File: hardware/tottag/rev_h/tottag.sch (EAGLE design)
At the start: 199 parts, among them J1 USB4110-GF-A, J2 DM3AT-SF-PEJM5, J3 TC2030-JLINK-NL-2SIDE, J4 TC2030-JLINK-NL-2SIDE, J5 MOLEX-PICO-SPOX-3SIDE, Q1 CSD75207W15, Q2 CSD75207W15, T1 HHM1595A1, U1 DW1000, U10 STM32F091CC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

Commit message: rev_h: split SPI buses; replace coil
Pin updates from SPI reconfiguration:

    SPI0 (Accelerometer)
        SCLK: P0.17
        MISO: P0.15
        MOSI: P0.13
        (INT, CS pins unchanged)
    SPI2 (RTC, SD Card)
        SCLK: P0.06
        MOSI: P0.07
        MISO: P0.05
        (CS, detect, etc pins unchanged)
    BATIN moved to P0.04 (to simplify routing)

---

Coil replaced with new part; slightly wider holes, adjusted fill to fit

(was meant to be its own commit; oh well)
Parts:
- L4: value WR222230-26M8-G -> WURTH_COIL_760308103204; device ac:WR222230-26M8-G -> ac:WURTH_COIL_760308103204
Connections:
- removed net NRF_MISO: J2.DATA0/MISO, R32.1, U11.SDO, U3.MISO/SA0, U7.P0.15
- removed net NRF_MOSI: J2.CMD/MOSI, R30.1, U11.SDI, U3.MOSI/SDA, U7.P0.13
- removed net NRF_SCK: J2.CLK, U11.SCL, U3.SCL/SPC, U7.P0.17
- new net NRF_SPI0_MISO: U3.MISO/SA0, U7.P0.15
- new net NRF_SPI0_MOSI: U3.MOSI/SDA, U7.P0.13
- new net NRF_SPI0_SCLK: U3.SCL/SPC, U7.P0.17
- new net NRF_SPI2_MISO: J2.DATA0/MISO, R32.1, U11.SDO, U7.P0.05/AIN3
- new net NRF_SPI2_MOSI: J2.CMD/MOSI, R30.1, U11.SDI, U7.P0.07
- new net NRF_SPI2_SCLK: J2.CLK, U11.SCL, U7.P0.06
- net BATIN: now also U7.P0.04/AIN2; no longer U7.P0.30*/AIN6
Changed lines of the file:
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@@
 <attribute name="MPN" value="GRM1555C1H471JA01J"/>
 </part>
-<part name="L4" library="ac" library_urn="urn:adsk.eagle:library:20878999" deviceset="WR222230-26M8-G" device="" package3d_urn="urn:adsk.eagle:package:20906931/3"/>
+<part name="L4" library="ac" library_urn="urn:adsk.eagle:library:20878999" deviceset="WURTH_COIL_760308103204" device="" package3d_urn="urn:adsk.eagle:package:26902695/1"/>
 <part name="R18" library="passives" library_urn="urn:adsk.eagle:library:20904581" deviceset="RESISTOR" device="0402_RES" package3d_urn="urn:adsk.eagle:package:20904668/2" value="5.1k">
 <attribute name="DIGIKEY" value="RMCF0402FT5K10CT-ND"/>
@@
 </segment>
 </net>
-<net name="NRF_MISO" class="0">
-<segment>
-<pinref part="U7" gate="G$1" pin="P0.15"/>
-<wire x1="60.96" y1="68.58" x2="55.88" y2="68.58" width="0.1524" layer="91"/>
-<label x="55.88" y="68.58" size="1.27" layer="95" rot="R180" xref="yes"/>
-</segment>
+<net name="NRF_SPI2_MISO" class="0">
 <segment>
 <pinref part="U11" gate="G$1" pin="SDO"/>
@@
 <label x="182.88" y="93.98" size="1.27" layer="95" rot="R180" xref="yes"/>
 </segment>
-</net>
-<net name="NRF_MOSI" class="0">
-<segment>
-<label x="55.88" y="73.66" size="1.27" layer="95" rot="R180" xref="yes"/>
-<pinref part="U7" gate="G$1" pin="P0.13"/>
-<wire x1="60.96" y1="73.66" x2="55.88" y2="73.66" width="0.1524" layer="91"/>
-</segment>
+<segment>
+<label x="111.76" y="124.46" size="1.27" layer="95" xref="yes"/>
+<wire x1="111.76" y1="124.46" x2="106.68" y2="124.46" width="0.1524" layer="91"/>
+<pinref part="U7" gate="G$1" pin="P0.05/AIN3"/>
+</segment>
+</net>
+<net name="NRF_SPI2_MOSI" class="0">
 <segment>
 <pinref part="U11" gate="G$1" pin="SDI"/>
@@
 <label x="182.88" y="91.44" size="1.27" layer="95" rot="R180" xref="yes"/>
 </segment>
-</net>
-<net name="NRF_SCK" class="0">
-<segment>
-<pinref part="U7" gate="G$1" pin="P0.17"/>
-<wire x1="60.96" y1="63.5" x2="55.88" y2="63.5" width="0.1524" layer="91"/>
-<label x="55.88" y="63.5" size="1.27" layer="95" rot="R180" xref="yes"/>
-</segment>
+<segment>
+<pinref part="U7" gate="G$1" pin="P0.07"/>
+<wire x1="55.88" y1="83.82" x2="60.96" y2="83.82" width="0.1524" layer="91"/>
+<label x="55.88" y="83.82" size="1.27" layer="95" rot="R180" xref="yes"/>
+</segment>
+</net>
+<net name="NRF_SPI2_SCLK" class="0">
 <segment>
 <pinref part="U11" gate="G$1" pin="SCL"/>
 <wire x1="187.96" y1="96.52" x2="182.88" y2="96.52" width="0.1524" layer="91"/>
 <label x="182.88" y="96.52" size="1.27" layer="95" rot="R180" xref="yes"/>
+</segment>
+<segment>
+<pinref part="U7" gate="G$1" pin="P0.06"/>
+<wire x1="55.88" y1="86.36" x2="60.96" y2="86.36" width="0.1524" layer="91"/>
+<label x="55.88" y="86.36" size="1.27" layer="95" rot="R180" xref="yes"/>
 </segment>
 </net>
@@
 <net name="BATIN" class="0">
 <segment>
-<pinref part="U7" gate="G$1" pin="P0.30*/AIN6"/>
-<wire x1="106.68" y1="116.84" x2="111.76" y2="116.84" width="0.1524" layer="91"/>
-<label x="111.76" y="116.84" size="1.27" layer="95" xref="yes"/>
+<label x="111.76" y="127" size="1.27" layer="95" xref="yes"/>
+<pinref part="U7" gate="G$1" pin="P0.04/AIN2"/>
+<wire x1="106.68" y1="127" x2="111.76" y2="127" width="0.1524" layer="91"/>
 </segment>
 </net>
@@
 <label x="55.88" y="78.74" size="1.27" layer="95" rot="R180" xref="yes"/>
 <pinref part="U7" gate="G$1" pin="P0.11"/>
+</segment>
+</net>
+<net name="NRF_SPI0_SCLK" class="0">
+<segment>
+<pinref part="U7" gate="G$1" pin="P0.17"/>
+<wire x1="55.88" y1="63.5" x2="60.96" y2="63.5" width="0.1524" layer="91"/>
+<label x="55.88" y="63.5" size="1.27" layer="95" rot="R180" xref="yes"/>
+</segment>
+</net>
+<net name="NRF_SPI0_MOSI" class="0">
+<segment>
+<pinref part="U7" gate="G$1" pin="P0.13"/>
+<wire x1="55.88" y1="73.66" x2="60.96" y2="73.66" width="0.1524" layer="91"/>
+<label x="55.88" y="73.66" size="1.27" layer="95" rot="R180" xref="yes"/>
+</segment>
+</net>
+<net name="NRF_SPI0_MISO" class="0">
+<segment>
+<pinref part="U7" gate="G$1" pin="P0.15"/>
+<wire x1="55.88" y1="68.58" x2="60.96" y2="68.58" width="0.1524" layer="91"/>
+<label x="55.88" y="68.58" size="1.27" layer="95" rot="R180" xref="yes"/>
 </segment>
 </net>
@@
 </segment>
 </net>
-<net name="NRF_MOSI" class="0">
-<segment>
-<pinref part="U3" gate="G$1" pin="MOSI/SDA"/>
-<wire x1="195.58" y1="35.56" x2="193.04" y2="35.56" width="0.1524" layer="91"/>
-<label x="193.04" y="35.56" size="1.27" layer="95" rot="R180" xref="yes"/>
-</segment>
+<net name="NRF_SPI2_MOSI" class="0">
 <segment>
 <pinref part="J2" gate="G$1" pin="CMD/MOSI"/>
@@
 </segment>
 </net>
-<net name="NRF_MISO" class="0">
-<segment>
-<pinref part="U3" gate="G$1" pin="MISO/SA0"/>
-<wire x1="195.58" y1="38.1" x2="193.04" y2="38.1" width="0.1524" layer="91"/>
-<label x="193.04" y="38.1" size="1.27" layer="95" rot="R180" xref="yes"/>
-</segment>
+<net name="NRF_SPI2_MISO" class="0">
 <segment>
 <pinref part="J2" gate="G$1" pin="DATA0/MISO"/>
@@
 </segment>
 </net>
-<net name="NRF_SCK" class="0">
-<segment>
-<pinref part="U3" gate="G$1" pin="SCL/SPC"/>
-<wire x1="195.58" y1="43.18" x2="193.04" y2="43.18" width="0.1524" layer="91"/>
-<label x="193.04" y="43.18" size="1.27" layer="95" rot="R180" xref="yes"/>
-</segment>
+<net name="NRF_SPI2_SCLK" class="0">
 <segment>
 <pinref part="J2" gate="G$1" pin="CLK"/>
@@
 </segment>
 </net>
+<net name="NRF_SPI0_SCLK" class="0">
+<segment>
+<pinref part="U3" gate="G$1" pin="SCL/SPC"/>
+<wire x1="193.04" y1="43.18" x2="195.58" y2="43.18" width="0.1524" layer="91"/>
+<label x="193.04" y="43.18" size="1.27" layer="95" rot="R180" xref="yes"/>
+</segment>
+</net>
+<net name="NRF_SPI0_MISO" class="0">
+<segment>
+<pinref part="U3" gate="G$1" pin="MISO/SA0"/>
+<wire x1="193.04" y1="38.1" x2="195.58" y2="38.1" width="0.1524" layer="91"/>
+<label x="193.04" y="38.1" size="1.27" layer="95" rot="R180" xref="yes"/>
+</segment>
+</net>
+<net name="NRF_SPI0_MOSI" class="0">
+<segment>
+<pinref part="U3" gate="G$1" pin="MOSI/SDA"/>
+<wire x1="193.04" y1="35.56" x2="195.58" y2="35.56" width="0.1524" layer="91"/>
+<label x="193.04" y="35.56" size="1.27" layer="95" rot="R180" xref="yes"/>
+</segment>
+</net>

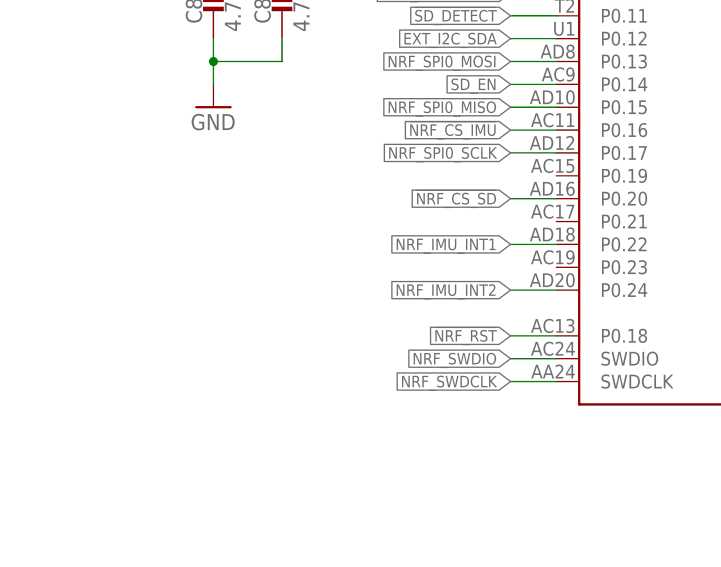
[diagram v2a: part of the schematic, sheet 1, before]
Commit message: rev_h: add board ID pins
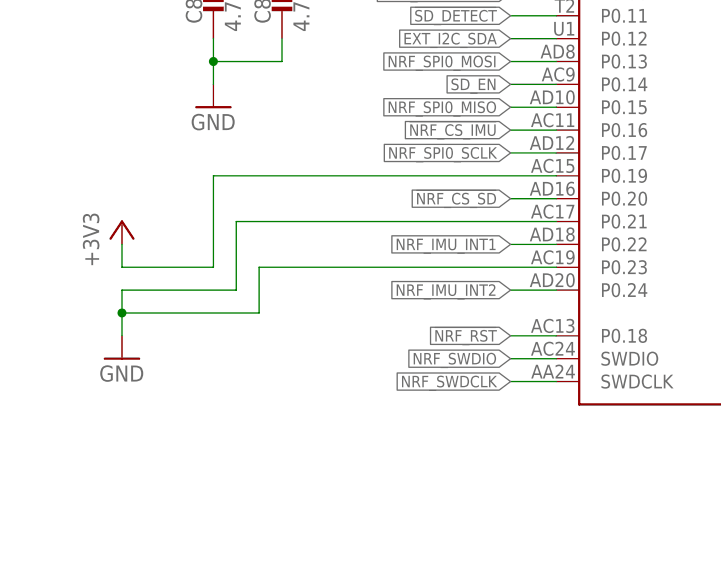
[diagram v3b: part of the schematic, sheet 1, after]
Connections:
- net +3V3: now also U7.P0.19
- net GND: now also U7.P0.21, U7.P0.23
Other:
- note added: "Board Revision ID Pins Rev H = 001"
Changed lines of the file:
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@@
 <part name="TP17" library="headers" deviceset="TEST-POINT" device=""/>
 <part name="TP18" library="headers" deviceset="TEST-POINT" device=""/>
+<part name="P+6" library="regulators" deviceset="+3V3" device=""/>
+<part name="GND9" library="supply1" library_urn="urn:adsk.eagle:library:371" deviceset="GND" device=""/>
 </parts>
 <sheets>
@@
 <text x="143.256" y="27.178" size="1.016" layer="98" align="top-left">Matching network from datasheet.
 Note v1.1 datasheet updated values.</text>
+<text x="11.176" y="34.798" size="1.016" layer="98" align="top-center">Board Revision ID Pins
+Rev H = 001
+</text>
+<wire x1="2.54" y1="30.48" x2="2.54" y2="58.42" width="0.1524" layer="98" style="longdash"/>
+<wire x1="19.304" y1="30.48" x2="19.304" y2="58.42" width="0.1524" layer="98" style="longdash"/>
+<wire x1="19.304" y1="30.48" x2="2.54" y2="30.48" width="0.1524" layer="98" style="longdash"/>
+<wire x1="19.304" y1="58.42" x2="2.54" y2="58.42" width="0.1524" layer="98" style="longdash"/>
 </plain>
 <instances>
@@
 <instance part="TP18" gate="G$1" x="213.36" y="170.18" smashed="yes" rot="R90">
 <attribute name="NAME" x="213.36" y="169.545" size="1.016" layer="95" ratio="12" rot="R90" align="center-right"/>
+</instance>
+<instance part="P+6" gate="P1" x="12.7" y="55.88" smashed="yes">
+<attribute name="VALUE" x="10.16" y="50.8" size="1.778" layer="96" rot="R90"/>
+</instance>
+<instance part="GND9" gate="1" x="12.7" y="40.64" smashed="yes">
+<attribute name="VALUE" x="10.16" y="38.1" size="1.778" layer="96"/>
 </instance>
 </instances>
@@
 <wire x1="30.48" y1="73.66" x2="22.86" y2="73.66" width="0.1524" layer="91"/>
 <junction x="22.86" y="73.66"/>
+</segment>
+<segment>
+<pinref part="U7" gate="G$1" pin="P0.23"/>
+<wire x1="60.96" y1="50.8" x2="27.94" y2="50.8" width="0.1524" layer="91"/>
+<wire x1="27.94" y1="50.8" x2="27.94" y2="45.72" width="0.1524" layer="91"/>
+<wire x1="27.94" y1="45.72" x2="12.7" y2="45.72" width="0.1524" layer="91"/>
+<pinref part="GND9" gate="1" pin="GND"/>
+<wire x1="12.7" y1="45.72" x2="12.7" y2="43.18" width="0.1524" layer="91"/>
+<pinref part="U7" gate="G$1" pin="P0.21"/>
+<wire x1="60.96" y1="55.88" x2="25.4" y2="55.88" width="0.1524" layer="91"/>
+<wire x1="25.4" y1="55.88" x2="25.4" y2="48.26" width="0.1524" layer="91"/>
+<wire x1="25.4" y1="48.26" x2="12.7" y2="48.26" width="0.1524" layer="91"/>
+<wire x1="12.7" y1="48.26" x2="12.7" y2="45.72" width="0.1524" layer="91"/>
+<junction x="12.7" y="45.72"/>
 </segment>
 </net>
@@
 <junction x="236.22" y="66.04"/>
 </segment>
+<segment>
+<pinref part="U7" gate="G$1" pin="P0.19"/>
+<wire x1="60.96" y1="60.96" x2="22.86" y2="60.96" width="0.1524" layer="91"/>
+<wire x1="22.86" y1="60.96" x2="22.86" y2="50.8" width="0.1524" layer="91"/>
+<wire x1="22.86" y1="50.8" x2="12.7" y2="50.8" width="0.1524" layer="91"/>
+<pinref part="P+6" gate="P1" pin="+3V3"/>
+<wire x1="12.7" y1="50.8" x2="12.7" y2="53.34" width="0.1524" layer="91"/>
+</segment>
 </net>

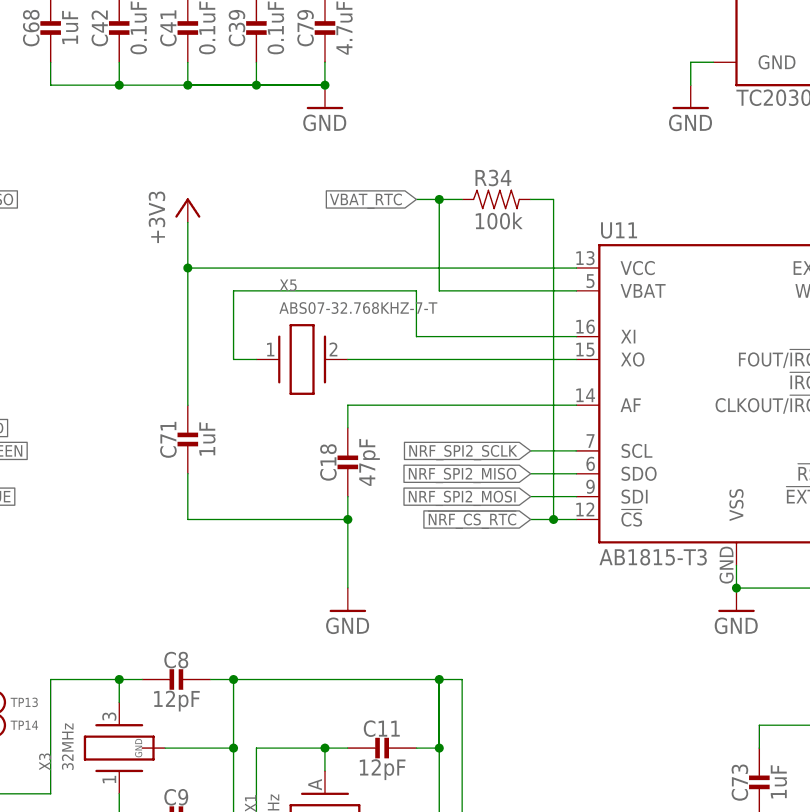
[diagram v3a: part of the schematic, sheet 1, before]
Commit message: rev_h: RTC CS pull-up to +3v3
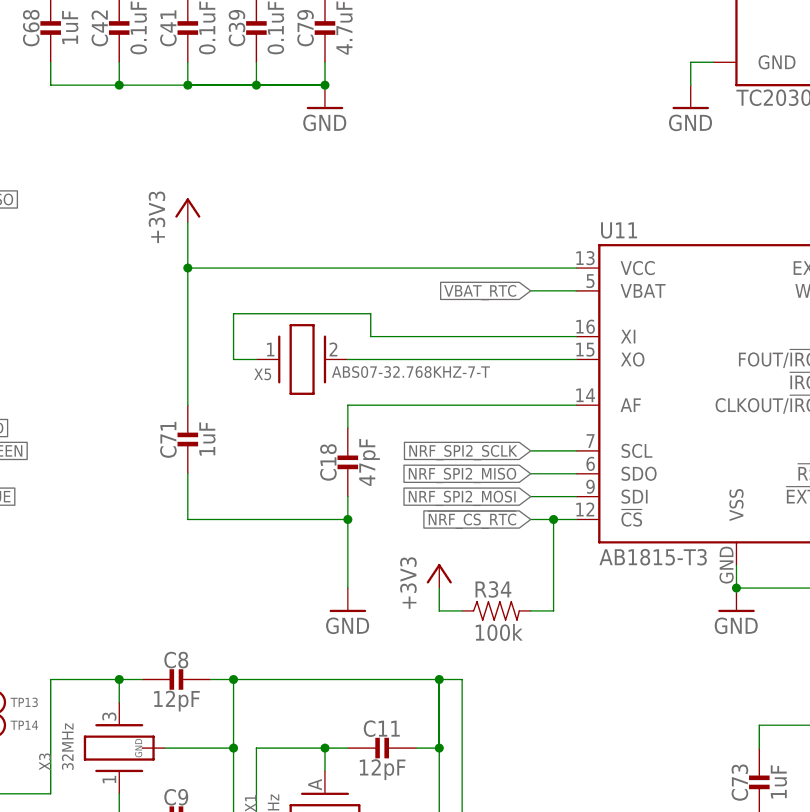
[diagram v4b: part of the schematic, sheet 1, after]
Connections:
- net +3V3: now also R34.1
- net VBAT_RTC: no longer R34.1
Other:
- moved on the sheet: R34
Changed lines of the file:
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@@
 <part name="P+6" library="regulators" deviceset="+3V3" device=""/>
 <part name="GND9" library="supply1" library_urn="urn:adsk.eagle:library:371" deviceset="GND" device=""/>
+<part name="P+7" library="regulators" deviceset="+3V3" device=""/>
 </parts>
 <sheets>
@@
 <wire x1="177.8" y1="165.1" x2="177.8" y2="129.54" width="0.1524" layer="98" style="longdash"/>
 <wire x1="177.8" y1="129.54" x2="254" y2="129.54" width="0.1524" layer="98" style="longdash"/>
-<text x="142.24" y="78.74" size="3.81" layer="98">RTC</text>
-<wire x1="177.8" y1="129.54" x2="134.62" y2="129.54" width="0.1524" layer="98" style="longdash"/>
-<wire x1="134.62" y1="129.54" x2="134.62" y2="74.93" width="0.1524" layer="98" style="longdash"/>
-<wire x1="134.62" y1="74.93" x2="254" y2="74.93" width="0.1524" layer="98" style="longdash"/>
+<text x="149.86" y="121.92" size="3.81" layer="98">RTC</text>
+<wire x1="177.8" y1="129.54" x2="137.16" y2="129.54" width="0.1524" layer="98" style="longdash"/>
+<wire x1="137.16" y1="129.54" x2="137.16" y2="74.93" width="0.1524" layer="98" style="longdash"/>
+<wire x1="137.16" y1="74.93" x2="254" y2="74.93" width="0.1524" layer="98" style="longdash"/>
 <text x="180.34" y="160.02" size="3.81" layer="98">J-LINK</text>
 <text x="178.816" y="166.37" size="3.81" layer="98">LED</text>
-<text x="190.5" y="124.968" size="1.778" layer="98">Pull-up nCS to prevent float</text>
+<text x="169.926" y="86.106" size="0.8128" layer="98">Pull-up nCS to prevent float</text>
 <text x="198.12" y="160.02" size="1.778" layer="98">x2 (top/bottom)</text>
 <text x="205.74" y="68.58" size="3.81" layer="98">Buzzer</text>
@@
 </instance>
 <instance part="X5" gate="G$1" x="157.48" y="106.68" smashed="yes">
-<attribute name="NAME" x="154.94" y="114.3" size="1.27" layer="95"/>
-<attribute name="VALUE" x="154.94" y="111.76" size="1.27" layer="96"/>
+<attribute name="NAME" x="154.178" y="105.664" size="1.27" layer="95" rot="R180"/>
+<attribute name="VALUE" x="160.782" y="104.648" size="1.27" layer="96"/>
 </instance>
 <instance part="C71" gate="G$1" x="144.78" y="99.06" smashed="yes">
@@
 <attribute name="MPN" x="238.76" y="58.42" size="1.27" layer="96" rot="R90" display="off"/>
 </instance>
-<instance part="R34" gate="G$1" x="180.34" y="124.46" smashed="yes">
-<attribute name="NAME" x="176.53" y="125.9586" size="1.778" layer="95"/>
-<attribute name="VALUE" x="176.53" y="121.158" size="1.778" layer="96"/>
+<instance part="R34" gate="G$1" x="180.34" y="78.74" smashed="yes">
+<attribute name="NAME" x="176.53" y="80.2386" size="1.778" layer="95"/>
+<attribute name="VALUE" x="176.53" y="75.438" size="1.778" layer="96"/>
 </instance>
 <instance part="A4" gate="G$1" x="185.42" y="48.26" smashed="yes">
@@
 <instance part="GND9" gate="1" x="12.7" y="40.64" smashed="yes">
 <attribute name="VALUE" x="10.16" y="38.1" size="1.778" layer="96"/>
+</instance>
+<instance part="P+7" gate="P1" x="172.72" y="83.82" smashed="yes">
+<attribute name="VALUE" x="170.18" y="78.74" size="1.778" layer="96" rot="R90"/>
 </instance>
 </instances>
@@
 <wire x1="12.7" y1="50.8" x2="12.7" y2="53.34" width="0.1524" layer="91"/>
 </segment>
+<segment>
+<pinref part="R34" gate="G$1" pin="1"/>
+<pinref part="P+7" gate="P1" pin="+3V3"/>
+<wire x1="175.26" y1="78.74" x2="172.72" y2="78.74" width="0.1524" layer="91"/>
+<wire x1="172.72" y1="78.74" x2="172.72" y2="81.28" width="0.1524" layer="91"/>
+</segment>
 </net>
 <net name="EXT_I2C_SDA" class="0">
@@
 <net name="N$41" class="0">
 <segment>
-<wire x1="149.86" y1="114.3" x2="170.18" y2="114.3" width="0.1524" layer="91"/>
-<wire x1="170.18" y1="114.3" x2="170.18" y2="109.22" width="0.1524" layer="91"/>
+<wire x1="149.86" y1="111.76" x2="165.1" y2="111.76" width="0.1524" layer="91"/>
+<wire x1="165.1" y1="111.76" x2="165.1" y2="109.22" width="0.1524" layer="91"/>
 <pinref part="U11" gate="G$1" pin="XI"/>
-<wire x1="170.18" y1="109.22" x2="187.96" y2="109.22" width="0.1524" layer="91"/>
+<wire x1="165.1" y1="109.22" x2="187.96" y2="109.22" width="0.1524" layer="91"/>
 <pinref part="X5" gate="G$1" pin="1"/>
-<wire x1="149.86" y1="114.3" x2="149.86" y2="106.68" width="0.1524" layer="91"/>
+<wire x1="149.86" y1="111.76" x2="149.86" y2="106.68" width="0.1524" layer="91"/>
 <wire x1="149.86" y1="106.68" x2="152.4" y2="106.68" width="0.1524" layer="91"/>
 </segment>
@@
 <label x="182.88" y="88.9" size="1.27" layer="95" rot="R180" xref="yes"/>
 <wire x1="185.42" y1="88.9" x2="182.88" y2="88.9" width="0.1524" layer="91"/>
-<wire x1="182.88" y1="124.46" x2="185.42" y2="124.46" width="0.1524" layer="91"/>
-<wire x1="185.42" y1="124.46" x2="185.42" y2="88.9" width="0.1524" layer="91"/>
+<wire x1="182.88" y1="78.74" x2="185.42" y2="78.74" width="0.1524" layer="91"/>
+<wire x1="185.42" y1="78.74" x2="185.42" y2="88.9" width="0.1524" layer="91"/>
 <junction x="185.42" y="88.9"/>
 <pinref part="R34" gate="G$1" pin="2"/>
@@
 <segment>
 <pinref part="U11" gate="G$1" pin="VBAT"/>
-<wire x1="187.96" y1="114.3" x2="172.72" y2="114.3" width="0.1524" layer="91"/>
-<wire x1="172.72" y1="114.3" x2="172.72" y2="124.46" width="0.1524" layer="91"/>
-<label x="170.18" y="124.46" size="1.27" layer="95" rot="R180" xref="yes"/>
-<wire x1="170.18" y1="124.46" x2="172.72" y2="124.46" width="0.1524" layer="91"/>
-<wire x1="175.26" y1="124.46" x2="172.72" y2="124.46" width="0.1524" layer="91"/>
-<junction x="172.72" y="124.46"/>
-<pinref part="R34" gate="G$1" pin="1"/>
-</segment>
-</net>
+<wire x1="187.96" y1="114.3" x2="182.88" y2="114.3" width="0.1524" layer="91"/>
+<label x="182.88" y="114.3" size="1.27" layer="95" rot="R180" xref="yes"/>
+</segment>
+</net>
